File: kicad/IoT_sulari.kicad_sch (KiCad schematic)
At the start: 1 part, among them U2 NRF9160-SICA-B1A-R

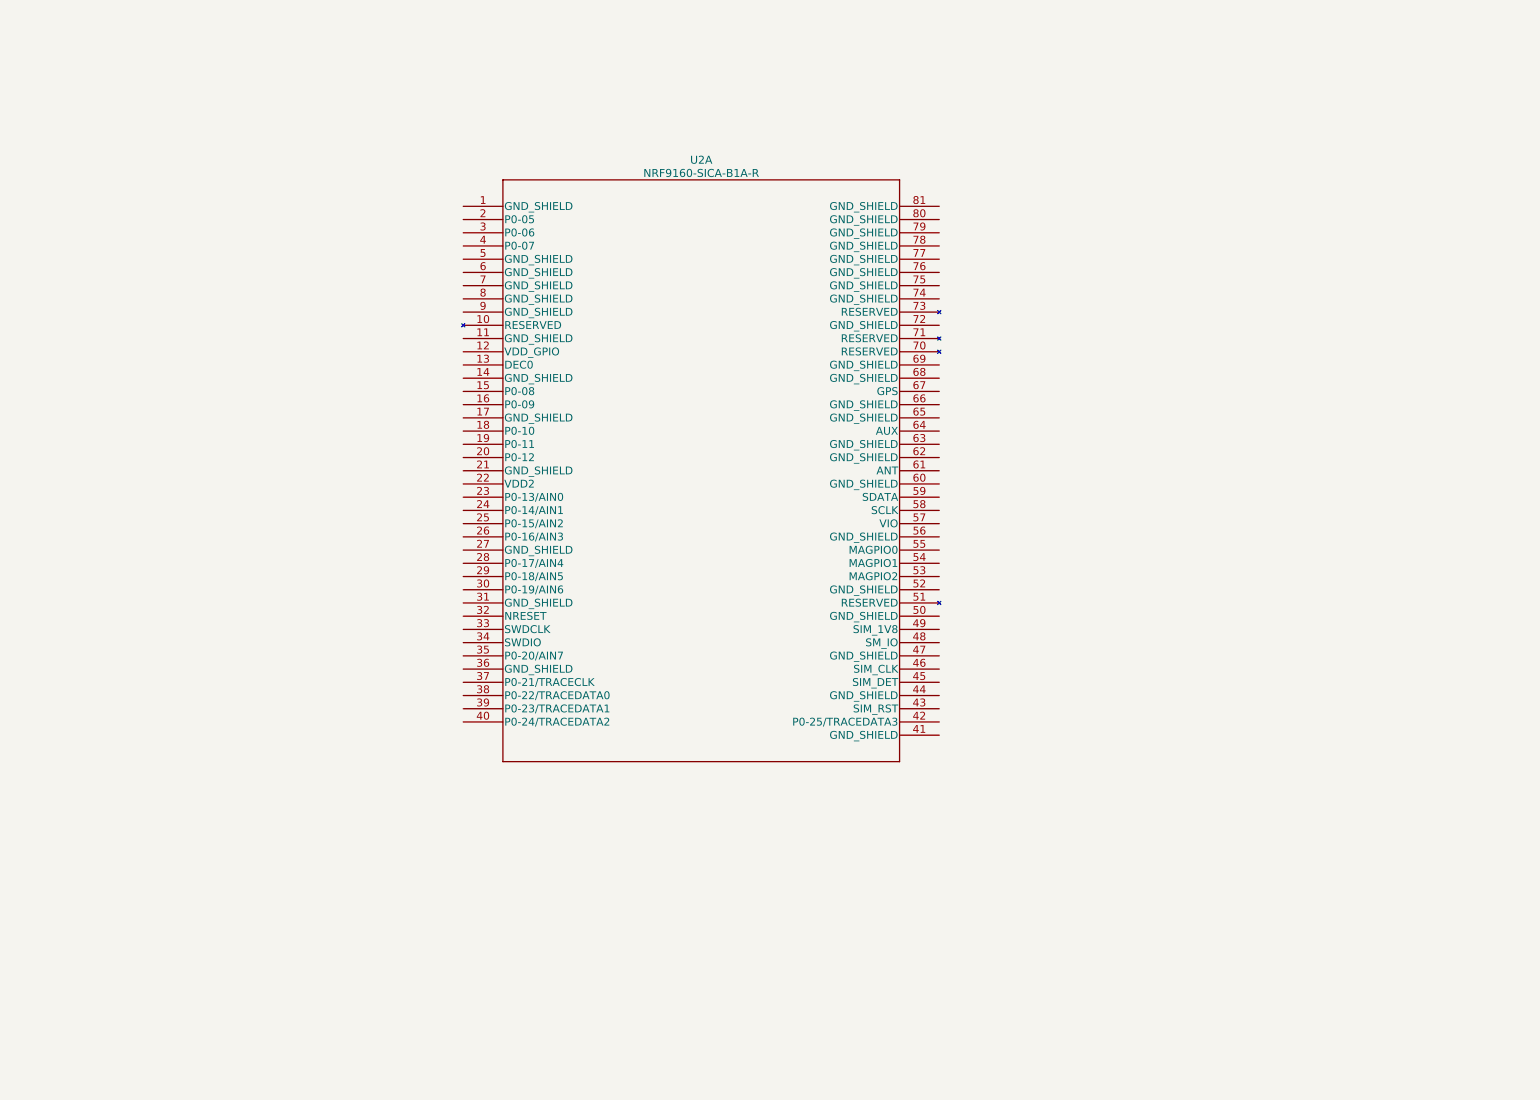
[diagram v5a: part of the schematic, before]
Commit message: Updated nrf9160 symbols for easier use, added sim card holder and doc, added first connections to mcu
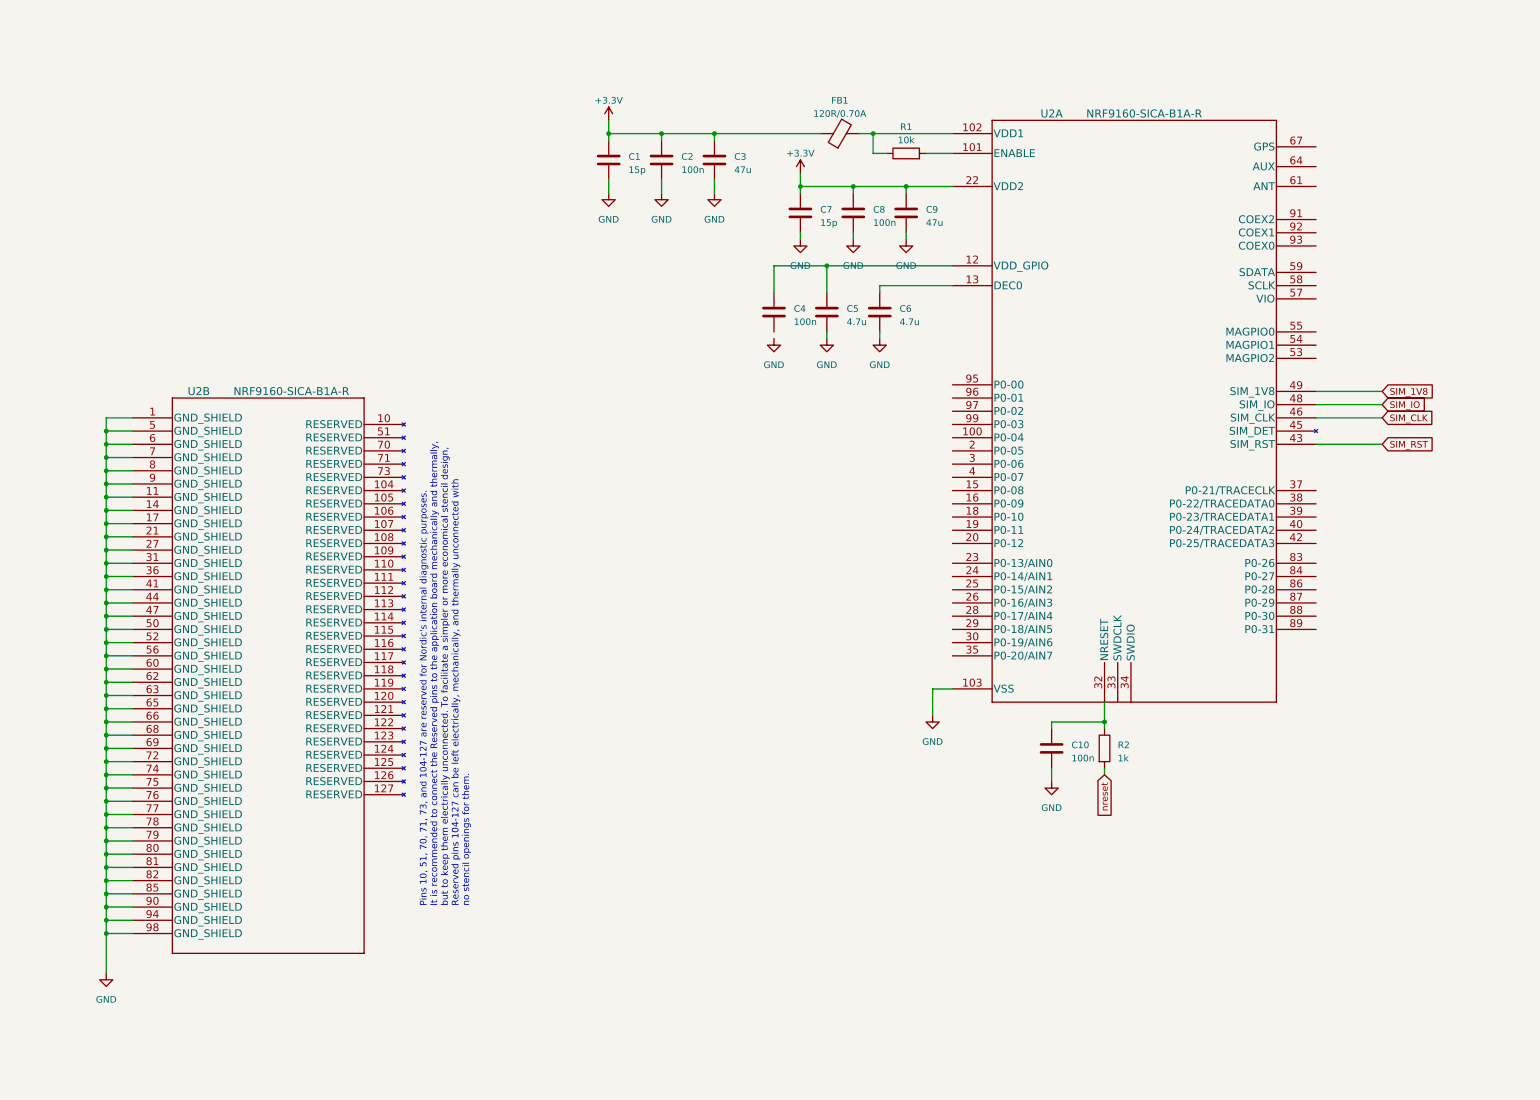
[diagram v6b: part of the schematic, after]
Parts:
- added C1, C7: 15p, symbol Device:C
- added C10, C2, C4, C8: 100n, symbol Device:C
- added C3, C9: 47u, symbol Device:C
- added C5, C6: 4.7u, symbol Device:C
- added FB1: 120R/0.70A, symbol Device:FerriteBead
- added R1: 10k, symbol Device:R
- added R2: 1k, symbol Device:R
- added unit 2 of U2
- U2: footprint NRF-9160-SICA-B1A-R:NRF9160-SICA-B1A-R -> LGA_16X10P5_NOR
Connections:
- net at U2.12 (VDD_GPIO): now also C4.1, C5.1
- net at U2.13 (DEC0): now also C6.1
- net +3.3V: now reaches U2.22 (VDD2)
- net +3.3V: now also C1.1, C2.1, C3.1, C7.1, C8.1, C9.1, FB1.1
- net at U2.32 (NRESET): now also C10.1, R2.1
- net SIM_RST: now reaches U2.43 (SIM_RST)
- net SIM_CLK: now reaches U2.46 (SIM_CLK)
- net SIM_IO: now reaches U2.48 (SIM_IO)
- net SIM_1V8: now reaches U2.49 (SIM_1V8)
- new net: R1.2, U2.101 (ENABLE)
- new net: FB1.2, R1.1, U2.102 (VDD1)
- new net GND: C1.2, C10.2, C2.2, C3.2, C5.2, C6.2, C7.2, C8.2, C9.2, U2.1 (GND_SHIELD), U2.103 (VSS), U2.11 (GND_SHIELD), U2.14 (GND_SHIELD), U2.17 (GND_SHIELD), U2.21 (GND_SHIELD), U2.27 (GND_SHIELD), U2.31 (GND_SHIELD), U2.36 (GND_SHIELD), U2.41 (GND_SHIELD), U2.44 (GND_SHIELD), U2.47 (GND_SHIELD), U2.5 (GND_SHIELD), U2.50 (GND_SHIELD), U2.52 (GND_SHIELD), U2.56 (GND_SHIELD), U2.6 (GND_SHIELD), U2.60 (GND_SHIELD), U2.62 (GND_SHIELD), U2.63 (GND_SHIELD), U2.65 (GND_SHIELD), U2.66 (GND_SHIELD), U2.68 (GND_SHIELD), U2.69 (GND_SHIELD), U2.7 (GND_SHIELD), U2.72 (GND_SHIELD), U2.74 (GND_SHIELD), U2.75 (GND_SHIELD), U2.76 (GND_SHIELD), U2.77 (GND_SHIELD), U2.78 (GND_SHIELD), U2.79 (GND_SHIELD), U2.8 (GND_SHIELD), U2.80 (GND_SHIELD), U2.81 (GND_SHIELD), U2.82 (GND_SHIELD), U2.85 (GND_SHIELD), U2.9 (GND_SHIELD), U2.90 (GND_SHIELD), U2.94 (GND_SHIELD), U2.98 (GND_SHIELD)
- new net nreset: R2.2
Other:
- note added: "Pins 10, 51, 70, 71, 73, and 104-127 are reserved for Nordic's internal diagnostic purposes. It is recommended to connect the Reserved pins to the application board mechanically and thermally, but to keep them electrically unconnected. To facilitate a simpler or more economical stencil design, Reserved pins 104-127 can be left electrically, mechanically, and thermally unconnected with no stencil 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"

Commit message: added power jack and usb connector
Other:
- added sheet USB_C_module (USB_C_module.kicad_sch)
- moved on the sheet: C1, C10, C2, C3, C4, C5, C6, C7, C8, C9, FB1, R1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

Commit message: Updated USB module
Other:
- company: (none) -> University of Oulu
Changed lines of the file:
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@@
 (kicad_sch (version 20230121) (generator eeschema)
   (paper "A4")
+  (title_block
+    (company "University of Oulu")
+  )
   (junction (at 20.32 124.46) (diameter 0) (color 0 0 0 0)
   )
